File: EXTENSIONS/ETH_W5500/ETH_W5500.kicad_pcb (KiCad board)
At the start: 2 copper layers, 59.5 x 34.3 mm, 69 parts, among them J1 EXT, J2 WE-634008137521, J3 MM-690367290876, U2 AZ1117IH-3.3, U3 W5500, Y1 25M

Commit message: feat: silkscreen labels, fiducials, gold finger fab note, v1.1.0
Main: EXT (J7) pinout labels, repo URL, hidden JLC order-number
placeholder under J7, J1 fab note (gold fingers yes, bevel not
possible), GOLD_FINGERS rule area, 3+3 fiducials. ETH: 3 bottom
fiducials (no room on top without moving parts). Revision v1.1.0.
DRC 0 errors on both boards.

Co-Authored-By: Claude Opus 5.5 <noreply@anthropic.com>
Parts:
- added FID1: Fiducial_1mm_Mask2mm, Fiducial_1mm_Mask2mm, B.Cu at (146.5, 106.2)
- added FID2: Fiducial_1mm_Mask2mm, Fiducial_1mm_Mask2mm, B.Cu at (164.5, 91.2)
- added FID3: Fiducial_1mm_Mask2mm, Fiducial_1mm_Mask2mm, B.Cu at (183.5, 107.2)

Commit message: feat(eth): silkscreen pinouts, LED legend, repo URL, JLC placeholder
EXT (J1) pin labels and J3 legend on bottom silk, LED function legend
(D10 duplex, D9 speed), repo URL, hidden JLC order-number placeholder
under TR1. DRC 0 errors.

Co-Authored-By: Claude Opus 5.5 <noreply@anthropic.com>
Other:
- board text added: "3V3"
- board text added: "5=3V3 6=5V 7,8=GND"
- board text added: "5V"
- board text added: "CS"
- board text added: "EXT (J1)"
- board text added: "GND"
- board text added: "INT"
- board text added: "J3: 1=A1 2=A2 3=B1 4=B2"
- board text added: "JLCJLCJLCJLC"
- board text added: "LED D10=DUP D9=SPD"
- board text added: "MI"
- board text added: "MO"
- board text added: "SCK"
- board text added: "SCL"
- board text added: "SDA"
- board text added: "github.com/the78mole/km271-wifi"
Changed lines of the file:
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@@
 			(at 4.651875 0.027763 0)
 			(layer "B.SilkS")
+			(hide yes)
 			(effects
 				(font
@@
 			(at 4.626875 0.077763 0)
 			(layer "B.SilkS")
+			(hide yes)
 			(effects
 				(font
@@
 			(at 4.601875 0.052763 0)
 			(layer "B.SilkS")
+			(hide yes)
 			(effects
 				(font
@@
 		(layer "User.7")
 	)
+	(gr_text "JLCJLCJLCJLC"
+		(at 175.75 101.17 0)
+		(layer "F.SilkS")
+		(effects
+			(font
+				(size 1 0.8)
+				(thickness 0.15)
+			)
+		)
+	)
 	(gr_text "5VSEL"
 		(at 190.948125 78.772237 0)
@@
 		)
 	)
+	(gr_text "5V"
+		(at 138.45 97.97 0)
+		(layer "B.SilkS")
+		(effects
+			(font
+				(size 1 0.8)
+				(thickness 0.15)
+			)
+			(justify mirror)
+		)
+	)
+	(gr_text "CS"
+		(at 138.45 100.51 0)
+		(layer "B.SilkS")
+		(effects
+			(font
+				(size 1 0.8)
+				(thickness 0.15)
+			)
+			(justify mirror)
+		)
+	)
+	(gr_text "MI"
+		(at 138.45 103.05 0)
+		(layer "B.SilkS")
+		(effects
+			(font
+				(size 1 0.8)
+				(thickness 0.15)
+			)
+			(justify mirror)
+		)
+	)
+	(gr_text "MO"
+		(at 138.45 105.59 0)
+		(layer "B.SilkS")
+		(effects
+			(font
+				(size 1 0.8)
+				(thickness 0.15)
+			)
+			(justify mirror)
+		)
+	)
+	(gr_text "SCK"
+		(at 138.45 108.13 0)
+		(layer "B.SilkS")
+		(effects
+			(font
+				(size 1 0.8)
+				(thickness 0.15)
+			)
+			(justify mirror)
+		)
+	)
+	(gr_text "EXT (J1)"
+		(at 141.65 95.6 0)
+		(layer "B.SilkS")
+		(effects
+			(font
+				(size 1 0.8)
+				(thickness 0.15)
+			)
+			(justify mirror)
+		)
+	)
+	(gr_text "3V3"
+		(at 144.85 97.97 0)
+		(layer "B.SilkS")
+		(effects
+			(font
+				(size 1 0.8)
+				(thickness 0.15)
+			)
+			(justify mirror)
+		)
+	)
+	(gr_text "SCL"
+		(at 144.85 100.51 0)
+		(layer "B.SilkS")
+		(effects
+			(font
+				(size 1 0.8)
+				(thickness 0.15)
+			)
+			(justify mirror)
+		)
+	)
+	(gr_text "SDA"
+		(at 144.85 103.05 0)
+		(layer "B.SilkS")
+		(effects
+			(font
+				(size 1 0.8)
+				(thickness 0.15)
+			)
+			(justify mirror)
+		)
+	)
+	(gr_text "INT"
+		(at 144.85 105.59 0)
+		(layer "B.SilkS")
+		(effects
+			(font
+				(size 1 0.8)
+				(thickness 0.15)
+			)
+			(justify mirror)
+		)
+	)
+	(gr_text "GND"
+		(at 144.85 108.13 0)
+		(layer "B.SilkS")
+		(effects
+			(font
+				(size 1 0.8)
+				(thickness 0.15)
+			)
+			(justify mirror)
+		)
+	)
+	(gr_text "LED D10=DUP D9=SPD"
+		(at 173 83.2 0)
+		(layer "B.SilkS")
+		(effects
+			(font
+				(size 1 0.8)
+				(thickness 0.15)
+			)
+			(justify mirror)
+		)
+	)
+	(gr_text "J3: 1=A1 2=A2 3=B1 4=B2"
+		(at 173 85.1 0)
+		(layer "B.SilkS")
+		(effects
+			(font
+				(size 1 0.8)
+				(thickness 0.15)
+			)
+			(justify mirror)
+		)
+	)
+	(gr_text "5=3V3 6=5V 7,8=GND"
+		(at 173 87 0)
+		(layer "B.SilkS")
+		(effects
+			(font
+				(size 1 0.8)
+				(thickness 0.15)
+			)
+			(justify mirror)
+		)
+	)
+	(gr_text "github.com/the78mole/km271-wifi"
+		(at 173 88.9 0)
+		(layer "B.SilkS")
+		(effects
+			(font
+				(size 1 0.8)
+				(thickness 0.15)
+			)
+			(justify mirror)
+		)
+	)

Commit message: feat(main): USB-C power input, 3D models for all parts, DRC/ERC warning cleanup
- J2 Mini-B -> HRO TYPE-C-31-M-12 (C165948), power only (D+/D- were
  unused): CC1/CC2 each 5k1 to GND (R69/R70, C23186), shield via R60
  as before. Local re-route around J2 only (scripts/jlc/usbc_swap.py),
  GND vias removed from under the metal shell. CPL offset verified
  against JLC footprint.
- 3D models in 3dmodels/ (project-relative): USB-C and TR1 from
  EasyEDA, stock B3SL/SOIC-8 for SW1-4/U3, approximate boxes for
  RJ45, WR-MM and WAGO (vendor models not available offline).
- Parity cleanup: power symbols instead of local GND/VBUS labels,
  PWR_FLAGs, SW1-4 footprint field, J8 not on board, fiducials
  board-only, field sync via netlist (includes excluded-from-BOM parts),
  ETH C25/C33 refdes, FID5 nudged. DRC 0 errors / 0 unconnected,
  ERC 0 errors on both boards.

Co-Authored-By: Claude Opus 5.5 <noreply@anthropic.com>
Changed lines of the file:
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@@
 		(embedded_fonts no)
 		(model "${USER_LIB_BASE}/userlibs/3dmodels/WE-690367290876.stp"
+			(hide yes)
 			(offset
 				(xyz 0 0 2.77)
@@
 			)
 		)
+		(model "${KIPRJMOD}/../../3dmodels/Wuerth_690367290876_WR-MM_approx.wrl"
+			(offset
+				(xyz 0 -0 0)
+			)
+			(scale
+				(xyz 1 1 1)
+			)
+			(rotate
+				(xyz 0 0 0)
+			)
+		)
 	)
 	(footprint "Capacitor_SMD:C_0603_1608Metric_Pad1.08x0.95mm_HandSolder"
@@
 				(font
 					(size 1.27 1.27)
+					(thickness 0.15)
 				)
 			)
@@
 		(tags "capacitor handsolder")
 		(property "Reference" "C33"
-			(at 0 -1.85 0)
+			(at -0.7875 1.9 0)
 			(layer "F.SilkS")
 			(effects
@@
 				(font
 					(size 1.27 1.27)
+					(thickness 0.15)
 				)
 			)
@@
 		(embedded_fonts no)
 		(model "${KICAD9_3DMODEL_DIR}/Transformer_SMD.3dshapes/Transformer_Ethernet_Wuerth_749013011A.wrl"
+			(hide yes)
 			(offset
 				(xyz 0 0 0)
@@
 			)
 		)
+		(model "${KIPRJMOD}/../../3dmodels/Wuerth_749013011A.step"
+			(offset
+				(xyz 0 -0.005 0)
+			)
+			(scale
+				(xyz 1 1 1)
+			)
+			(rotate
+				(xyz 0 0 270)
+			)
+		)
 	)
 	(footprint "LED_SMD:LED_0603_1608Metric_Pad1.05x0.95mm_HandSolder"
@@
 		(embedded_fonts no)
 		(model "${PATH_3D_THE78MOLE}/WE-MJ-634008137521.stp"
+			(hide yes)
 			(offset
 				(xyz 0 2.44 6.91)
@@
 			)
 		)
+		(model "${KIPRJMOD}/../../3dmodels/Wuerth_634008137521_RJ45_approx.wrl"
+			(offset
+				(xyz -0.0000000000000004 3.4375 0)
+			)
+			(scale
+				(xyz 1 1 1)
+			)
+			(rotate
+				(xyz 0 0 0)
+			)
+		)
 	)
 	(footprint "Inductor_SMD:L_0603_1608Metric_Pad1.05x0.95mm_HandSolder"
@@
 		(tags "capacitor handsolder")
 		(property "Reference" "C25"
-			(at 2.8625 0 0)
+			(at 2.914375 0 0)
 			(layer "F.SilkS")
 			(effects
 				(font
-					(size 0.8 0.8)
-					(thickness 0.13)
+					(size 1 1)
+					(thickness 0.15)
 				)
 			)
@@
 			)
 		)
-		(attr smd exclude_from_pos_files exclude_from_bom)
+		(attr smd board_only exclude_from_pos_files exclude_from_bom)
 		(duplicate_pad_numbers_are_jumpers no)
 		(fp_circle
@@
 			)
 		)
-		(attr smd exclude_from_pos_files exclude_from_bom)
+		(attr smd board_only exclude_from_pos_files exclude_from_bom)
 		(duplicate_pad_numbers_are_jumpers no)
 		(fp_circle
@@
 			)
 		)
-		(attr smd exclude_from_pos_files exclude_from_bom)
+		(attr smd board_only exclude_from_pos_files exclude_from_bom)
 		(duplicate_pad_numbers_are_jumpers no)
 		(fp_circle

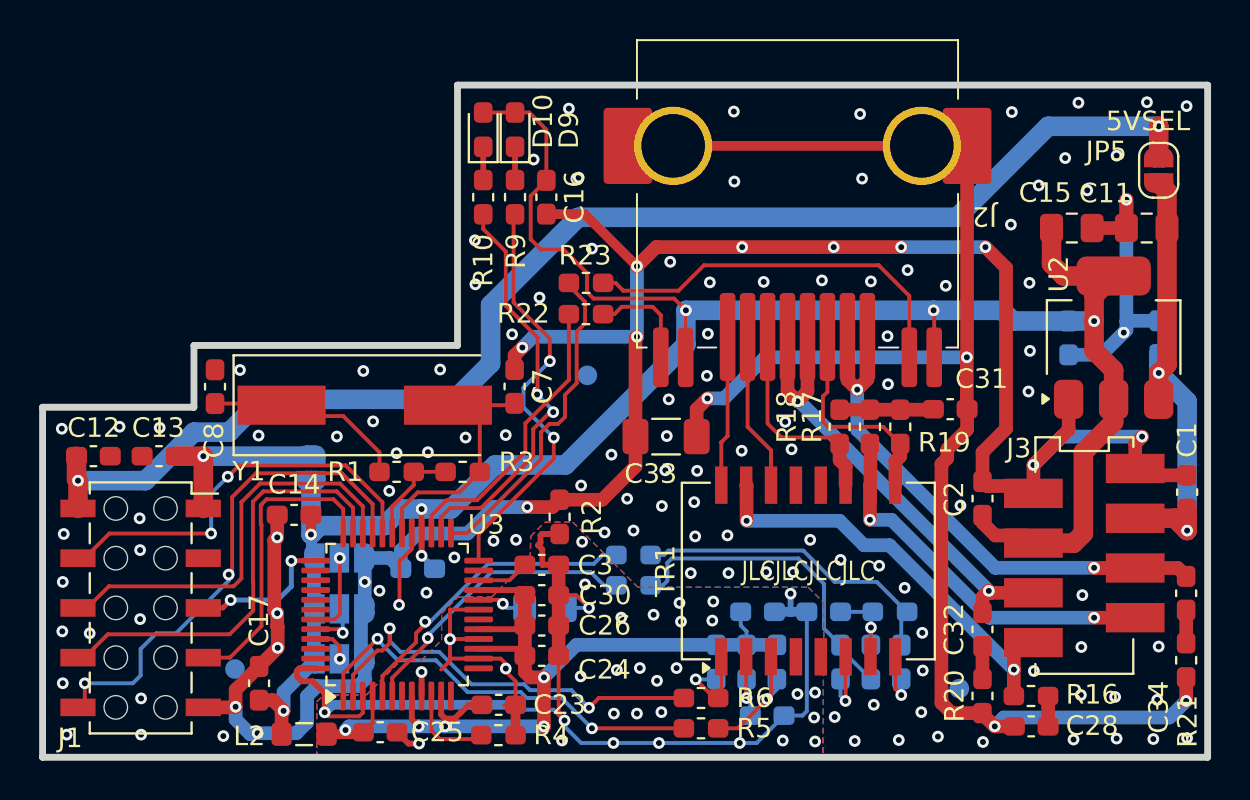
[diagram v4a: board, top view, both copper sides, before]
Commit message: fix: LED silkscreen order, visible refdes, fab notes, pour pullback
- Main: LED labels were reversed vs. nets (D1=IO21 ... D4=IO25); fixed.
- All refdes visible (R10, H1, ETH JP1-3 placed instead of hidden).
- ETH fiducials restored/placed clear of JP1 text and copper.
- Fab notes (stackup, finish, gold finger, assembly) on Cmts.User.
- Copper pours pulled back 0.5 mm from routed edges (zone-only rule).
- scripts/jlc/verify.py: pin-level netlist diff vs upstream, placement
  diff, BOM/CPL/PCB refdes consistency, hidden refdes, connector nets.

Co-Authored-By: Claude Opus 5.5 <noreply@anthropic.com>
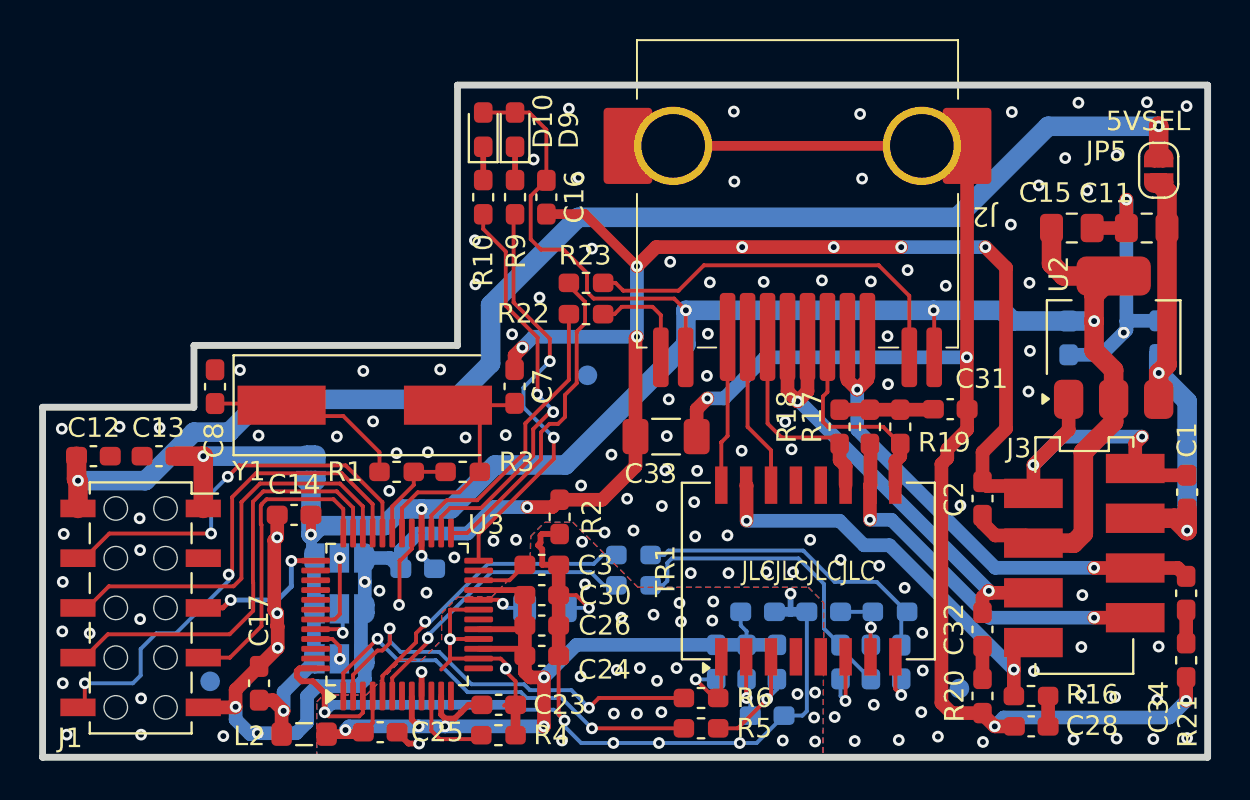
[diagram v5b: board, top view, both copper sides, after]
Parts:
- moved FID1 1.41 mm to (145.2, 106.8)
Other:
- board text added: "FAB NOTES ${TITLE} rev ${REVISION} Stackup: 2 layers, FR4 TG135, 1.6 mm +-10 pct, outer copper 1 oz (35 um) L1 F.Cu signal/GND pour | core 1.5 mm | L2 B.Cu signal/GND pour Finish: HASL lead-free. Gold fingers: no Mask green, silk white, vias tented. Min track/space 0.20/0.20 mm, min via 0.3/0.6 mm Assembly: Standard PCBA, both sides. BOM/CPL: production/bom.csv, production/positions.csv"
